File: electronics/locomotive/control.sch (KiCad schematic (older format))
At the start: 23 parts

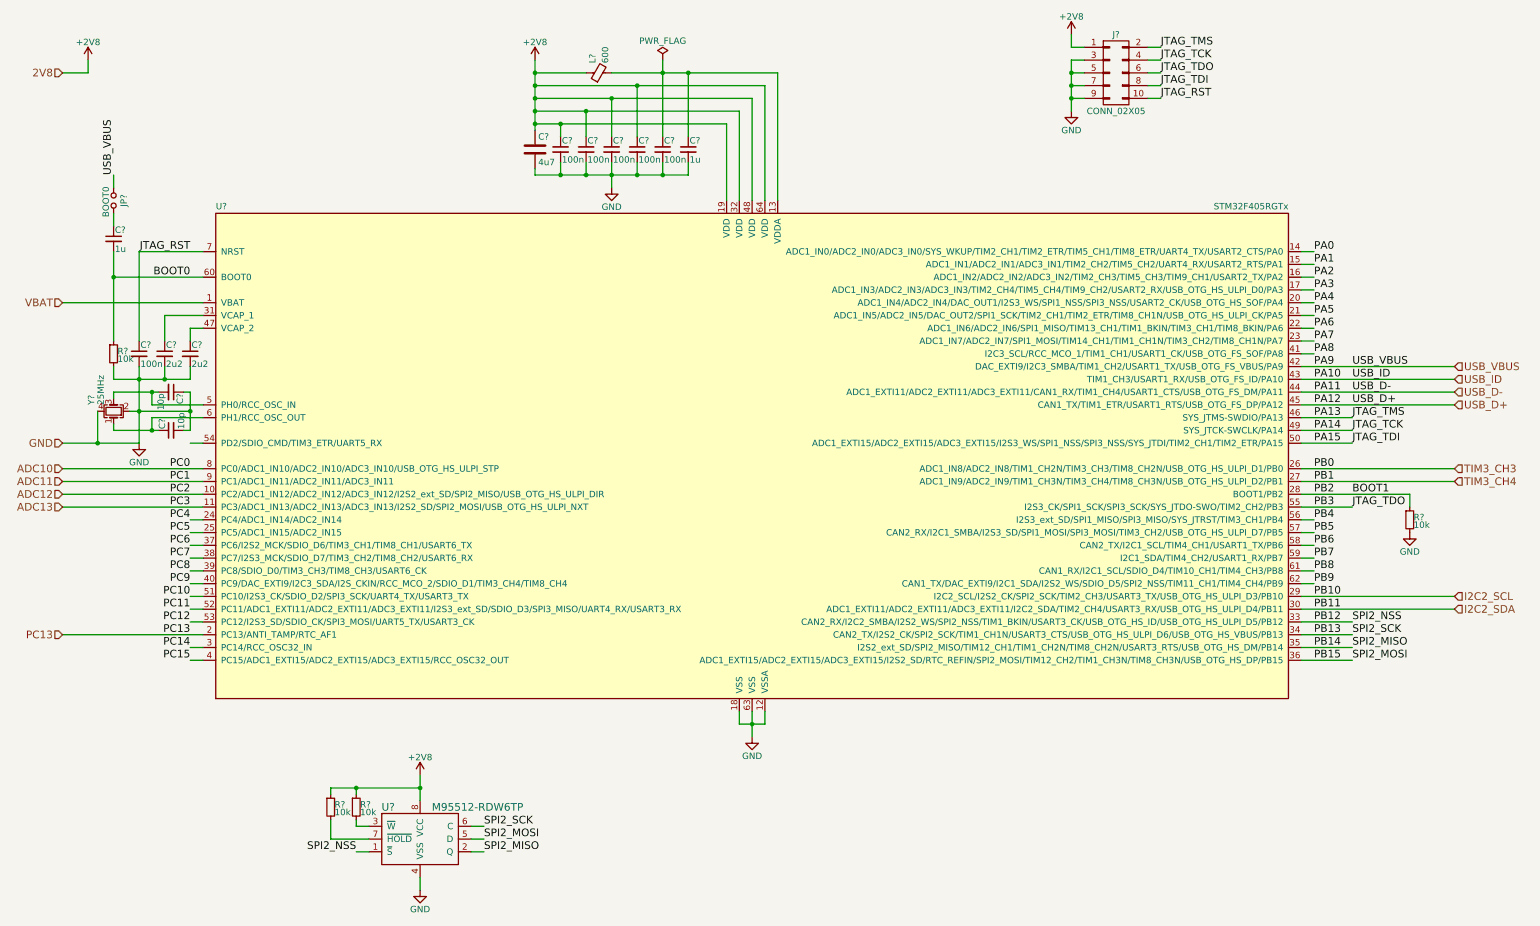
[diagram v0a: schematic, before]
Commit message: electronics: locomotive: Update schematics
Voltage regulator, TOF, IR receiver, voltage scaler, I2C control lines, power
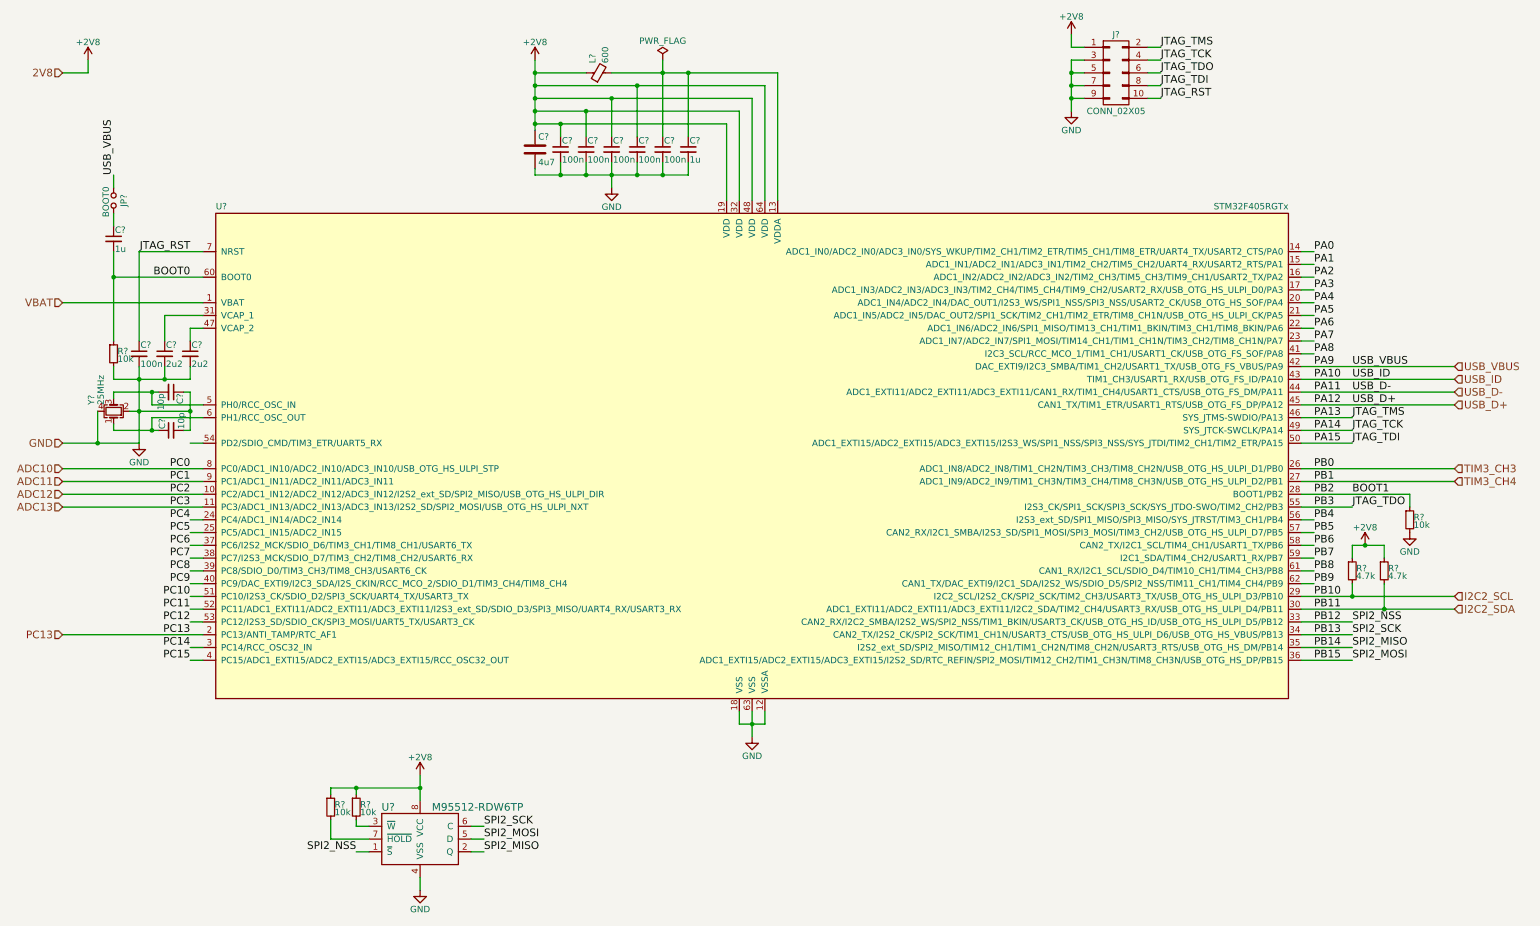
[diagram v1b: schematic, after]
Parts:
- added R? (x2): 4.7k, symbol R_Small
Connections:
- net +2V8: now also R?.1, R?.1
- net I2C2_SCL: now also R?.2
- net I2C2_SDA: now also R?.2
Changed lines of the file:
@@
 LIBS:valves
 LIBS:stm32
+LIBS:SPX3819
 LIBS:bcan
+LIBS:TSOP57238
 LIBS:locomotive-cache
 EELAYER 25 0
@@
 $EndComp
 $Comp
-L GND #PWR03
+L GND #PWR019
 U 1 1 58AFF73E
 P 5800 6300
-F 0 "#PWR03" H 5800 6050 50  0001 C CNN
+F 0 "#PWR019" H 5800 6050 50  0001 C CNN
 F 1 "GND" H 5800 6150 50  0000 C CNN
 F 2 "" H 5800 6300 50  0001 C CNN
@@
 $EndComp
 $Comp
-L +2V8 #PWR04
+L +2V8 #PWR020
 U 1 1 58AFF779
 P 4100 1000
-F 0 "#PWR04" H 4100 850 50  0001 C CNN
+F 0 "#PWR020" H 4100 850 50  0001 C CNN
 F 1 "+2V8" H 4100 1140 50  0000 C CNN
 F 2 "" H 4100 1000 50  0001 C CNN
@@
 $EndComp
 $Comp
-L GND #PWR05
+L GND #PWR021
 U 1 1 58B09824
 P 4700 2000
-F 0 "#PWR05" H 4700 1750 50  0001 C CNN
+F 0 "#PWR021" H 4700 1750 50  0001 C CNN
 F 1 "GND" H 4700 1850 50  0000 C CNN
 F 2 "" H 4700 2000 50  0001 C CNN
@@
 $EndComp
 $Comp
-L PWR_FLAG #FLG06
+L PWR_FLAG #FLG022
 U 1 1 58B0A0B9
 P 5100 1000
-F 0 "#FLG06" H 5100 1075 50  0001 C CNN
+F 0 "#FLG022" H 5100 1075 50  0001 C CNN
 F 1 "PWR_FLAG" H 5100 1150 50  0000 C CNN
 F 2 "" H 5100 1000 50  0001 C CNN
@@
 $EndComp
 $Comp
-L GND #PWR07
+L GND #PWR023
 U 1 1 58B0A8F2
 P 1000 4000
-F 0 "#PWR07" H 1000 3750 50  0001 C CNN
+F 0 "#PWR023" H 1000 3750 50  0001 C CNN
 F 1 "GND" H 1000 3850 50  0000 C CNN
 F 2 "" H 1000 4000 50  0001 C CNN
@@
 BOOT1
 $Comp
-L GND #PWR?
+L GND #PWR024
 U 1 1 58B1062C
 P 10950 4700
-F 0 "#PWR?" H 10950 4450 50  0001 C CNN
+F 0 "#PWR024" H 10950 4450 50  0001 C CNN
 F 1 "GND" H 10950 4550 50  0000 C CNN
 F 2 "" H 10950 4700 50  0001 C CNN
@@
 $EndComp
 $Comp
-L GND #PWR?
+L GND #PWR025
 U 1 1 58B0F133
 P 8300 1400
-F 0 "#PWR?" H 8300 1150 50  0001 C CNN
+F 0 "#PWR025" H 8300 1150 50  0001 C CNN
 F 1 "GND" H 8300 1250 50  0000 C CNN
 F 2 "" H 8300 1400 50  0001 C CNN
@@
 $EndComp
 $Comp
-L +2V8 #PWR?
+L +2V8 #PWR026
 U 1 1 58B0F3EA
 P 8300 800
-F 0 "#PWR?" H 8300 650 50  0001 C CNN
+F 0 "#PWR026" H 8300 650 50  0001 C CNN
 F 1 "+2V8" H 8300 940 50  0000 C CNN
 F 2 "" H 8300 800 50  0001 C CNN
@@
 SPI2_MOSI
 $Comp
-L +2V8 #PWR?
+L +2V8 #PWR027
 U 1 1 58B14B55
 P 3200 6600
-F 0 "#PWR?" H 3200 6450 50  0001 C CNN
+F 0 "#PWR027" H 3200 6450 50  0001 C CNN
 F 1 "+2V8" H 3200 6740 50  0000 C CNN
 F 2 "" H 3200 6600 50  0001 C CNN
@@
 $EndComp
 $Comp
-L GND #PWR?
+L GND #PWR028
 U 1 1 58B14B8F
 P 3200 7500
-F 0 "#PWR?" H 3200 7250 50  0001 C CNN
+F 0 "#PWR028" H 3200 7250 50  0001 C CNN
 F 1 "GND" H 3200 7350 50  0000 C CNN
 F 2 "" H 3200 7500 50  0001 C CNN
@@
 2V8
 $Comp
-L +2V8 #PWR?
+L +2V8 #PWR029
 U 1 1 58B16608
 P 600 1000
-F 0 "#PWR?" H 600 850 50  0001 C CNN
+F 0 "#PWR029" H 600 850 50  0001 C CNN
 F 1 "+2V8" H 600 1140 50  0000 C CNN
 F 2 "" H 600 1000 50  0001 C CNN
@@
 Connection ~ 675  4000
 Wire Wire Line
-	1000 3400 1000 4000
+	1000 4000 1000 3400
 Wire Wire Line
 	3600 7200 3700 7200
@@
 Connection ~ 8300 1300
 Wire Wire Line
-	8400 1200 8300 1200
+	8300 1200 8400 1200
 Wire Wire Line
 	8300 1000 8300 1400
@@
 	1500 2900 400  2900
 Wire Wire Line
-	1000 4000 400  4000
+	400  4000 1000 4000
 Wire Wire Line
 	675  3750 675  4000
@@
 Connection ~ 5100 1900
 Wire Wire Line
-	5100 1800 5100 1900
+	5100 1900 5100 1800
 Connection ~ 4900 1900
 Wire Wire Line
-	4900 1800 4900 1900
+	4900 1900 4900 1800
 Connection ~ 4700 1900
 Wire Wire Line
@@
 Connection ~ 4500 1900
 Wire Wire Line
-	4500 1800 4500 1900
+	4500 1900 4500 1800
 Connection ~ 4300 1900
 Wire Wire Line
@@
 Wire Wire Line
 	5700 6100 5700 6200
+$Comp
+L R_Small R?
+U 1 1 58C3873D
+P 10500 5000
+F 0 "R?" H 10530 5020 50  0000 L CNN
+F 1 "4.7k" H 10530 4960 50  0000 L CNN
+F 2 "" H 10500 5000 50  0001 C CNN
+F 3 "" H 10500 5000 50  0001 C CNN
+	1    10500 5000
+	1    0    0    -1
+$EndComp
+$Comp
+L R_Small R?
+U 1 1 58C38817
+P 10750 5000
+F 0 "R?" H 10780 5020 50  0000 L CNN
+F 1 "4.7k" H 10780 4960 50  0000 L CNN
+F 2 "" H 10750 5000 50  0001 C CNN
+F 3 "" H 10750 5000 50  0001 C CNN
+	1    10750 5000
+	1    0    0    -1
+$EndComp
+$Comp
+L +2V8 #PWR030
+U 1 1 58C38DA2
+P 10600 4800
+F 0 "#PWR030" H 10600 4650 50  0001 C CNN
+F 1 "+2V8" H 10600 4940 50  0000 C CNN
+F 2 "" H 10600 4800 50  0001 C CNN
+F 3 "" H 10600 4800 50  0001 C CNN
+	1    10600 4800
+	1    0    0    -1
+$EndComp
+Wire Wire Line
+	10500 4800 10750 4800
+Wire Wire Line
+	10500 4800 10500 4900
+Wire Wire Line
+	10750 4800 10750 4900
+Connection ~ 10600 4800
+Wire Wire Line
+	10750 5100 10750 5300
+Connection ~ 10750 5300
+Wire Wire Line
+	10500 5100 10500 5200
+Connection ~ 10500 5200
 $EndSCHEMATC
